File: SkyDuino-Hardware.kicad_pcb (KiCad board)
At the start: 4 copper layers, 123 x 56 mm, 75 parts, among them J1 24V, J11 DBG, J12 USB-A RMT, J13 DISP, J14 USB_C Artisan, J2 BT, J4 Drum, J5 Exhaust, J6 Cooling, J7 Cooling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

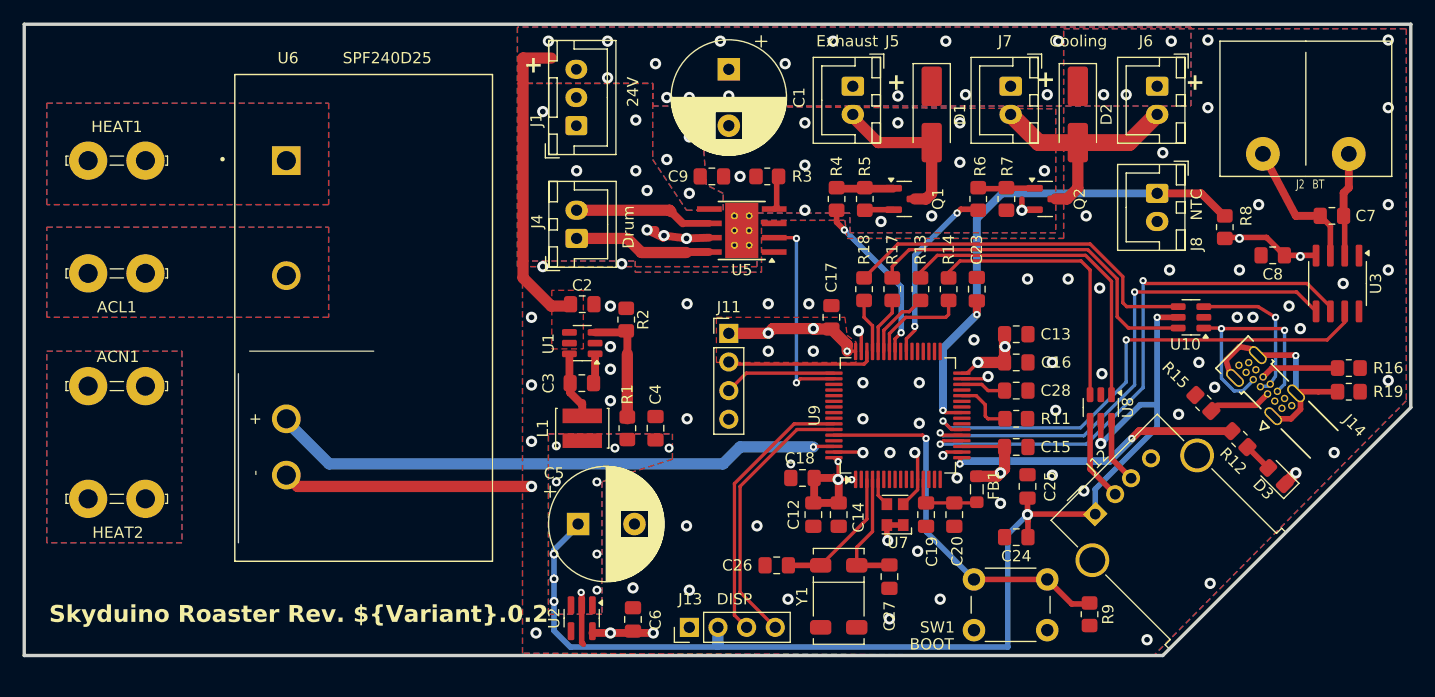
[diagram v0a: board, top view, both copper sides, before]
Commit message: Refactor power rail and optimize pours
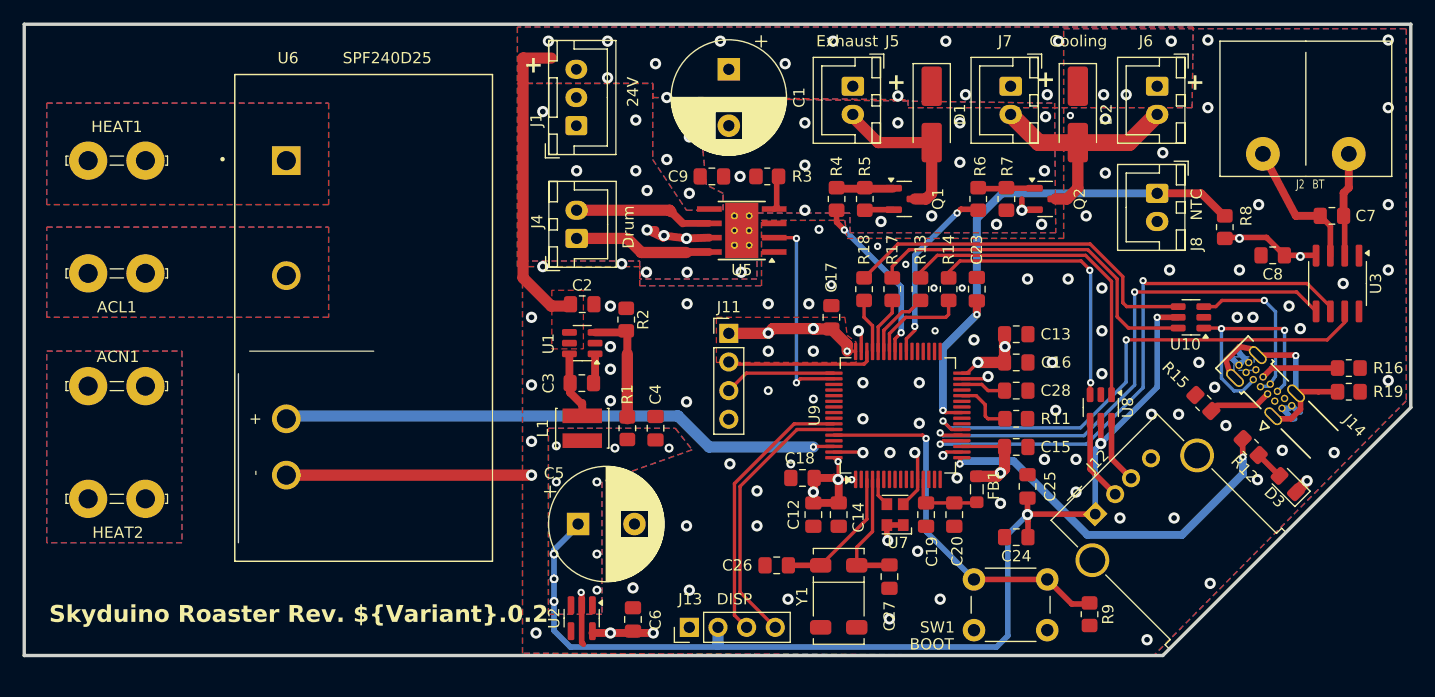
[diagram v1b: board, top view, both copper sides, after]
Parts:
- moved D3 1.22 mm to (218.1, 120.8)
- moved R12 1.22 mm to (214.8, 117.5)
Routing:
- net LED0: track 25.9 -> 33.9 mm
- net +5V: track 104.6 -> 97.6 mm
- net GND: track 52.7 -> 58.5 mm, vias 89 -> 117
- net SSR: track 51.0 -> 49.8 mm
- net /CPU/D+: track 13.7 -> 14.6 mm
- net Net-(R14-Pad1): vias 0 -> 2
- net +3V3: vias 16 -> 17
- net +24V: vias 21 -> 19

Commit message: Move SSR GND connection to B layer
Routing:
- net GND: vias 117 -> 119
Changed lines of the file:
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@@
 		)
 	)
+	(dimension
+		(type aligned)
+		(layer "F.Cu")
+		(pts
+			(xy 229 80) (xy 229 114)
+		)
+		(height -4.6)
+		(gr_text "34.0000 mm"
+			(at 231.8 97 90)
+			(layer "F.Cu")
+			(effects
+				(font
+					(size 1.5 1.5)
+					(thickness 0.3)
+				)
+			)
+		)
+		(format
+			(prefix "")
+			(suffix "")
+			(units 3)
+			(units_format 1)
+			(precision 4)
+		)
+		(style
+			(thickness 0.2)
+			(arrow_length 1.27)
+			(text_position_mode 0)
+			(extension_height 0.58642)
+			(extension_offset 0.5) keep_text_aligned)
+	)
+	(dimension
+		(type aligned)
+		(layer "F.Cu")
+		(pts
+			(xy 207.114627 135.504071) (xy 106 136)
+		)
+		(height -4.964587)
+		(gr_text "101.1158 mm"
+			(at 156.572834 138.916585 0.2810124376)
+			(layer "F.Cu")
+			(effects
+				(font
+					(size 1.5 1.5)
+					(thickness 0.3)
+				)
+			)
+		)
+		(format
+			(prefix "")
+			(suffix "")
+			(units 3)
+			(units_format 1)
+			(precision 4)
+		)
+		(style
+			(thickness 0.2)
+			(arrow_length 1.27)
+			(text_position_mode 0)
+			(extension_height 0.58642)
+			(extension_offset 0.5) keep_text_aligned)
+	)
+	(dimension
+		(type aligned)
+		(layer "F.Cu")
+		(pts
+			(xy 106 80) (xy 229 80)
+		)
+		(height -5)
+		(gr_text "123.0000 mm"
+			(at 167.5 73.2 0)
+			(layer "F.Cu")
+			(effects
+				(font
+					(size 1.5 1.5)
+					(thickness 0.3)
+				)
+			)
+		)
+		(format
+			(prefix "")
+			(suffix "")
+			(units 3)
+			(units_format 1)
+			(precision 4)
+		)
+		(style
+			(thickness 0.2)
+			(arrow_length 1.27)
+			(text_position_mode 0)
+			(extension_height 0.58642)
+			(extension_offset 0.5) keep_text_aligned)
+	)
+	(dimension
+		(type aligned)
+		(layer "F.Cu")
+		(pts
+			(xy 106 80) (xy 106 136)
+		)
+		(height 6.6)
+		(gr_text "56.0000 mm"
+			(at 97.6 108 90)
+			(layer "F.Cu")
+			(effects
+				(font
+					(size 1.5 1.5)
+					(thickness 0.3)
+				)
+			)
+		)
+		(format
+			(prefix "")
+			(suffix "")
+			(units 3)
+			(units_format 1)
+			(precision 4)
+		)
+		(style
+			(thickness 0.2)
+			(arrow_length 1.27)
+			(text_position_mode 0)
+			(extension_height 0.58642)
+			(extension_offset 0.5) keep_text_aligned)
+	)
 	(segment
 		(start 111.67 122.1)
@@
 	)
 	(segment
-		(start 151 120)
-		(end 129.25 120)
-		(width 1)
-		(layer "F.Cu")
-		(net 3)
-	)
-	(segment
 		(start 164.75 99)
 		(end 162.75 98.75)
@@
 	)
 	(via
+		(at 151 129)
+		(size 1)
+		(drill 0.5)
+		(layers "F.Cu" "B.Cu")
+		(free yes)
+		(net 3)
+	)
+	(via
 		(at 165 130.2)
 		(size 1)
@@
 	)
 	(via
+		(at 151 124)
+		(size 1)
+		(drill 0.5)
+		(layers "F.Cu" "B.Cu")
+		(free yes)
+		(net 3)
+	)
+	(via
 		(at 189.2 103.4)
 		(size 0.65)
@@
 	)
 	(segment
+		(start 151 120)
+		(end 129.25 120)
+		(width 1)
+		(layer "B.Cu")
+		(net 3)
+	)
+	(segment
 		(start 217.568377 114.068376)
 		(end 218.500001 115)
@@
 	)
 	(zone
-		(net 3)
-		(net_name "GND")
-		(layer "F.Cu")
-		(name "$teardrop_padvia$")
-		(hatch full 0.1)
-		(priority 30000)
-		(attr
-			(teardrop
-				(type padvia)
-			)
-		)
-		(connect_pads yes
-			(clearance 0)
-		)
-		(min_thickness 0.0254)
-		(filled_areas_thickness no)
-		(fill yes
-			(thermal_gap 0.5)
-			(thermal_bridge_width 0.5)
-			(island_removal_mode 1)
-			(island_area_min 10)
-		)
-		(polygon
-			(pts
-				(xy 131.525 120.5) (xy 131.525 119.5) (xy 130.011659 119) (xy 129.249 120) (xy 130.011659 121)
-			)
-		)
-	)
-	(zone
 		(net 10)
 		(net_name "Net-(J2-Pin_2)")
@@
 	)
 	(zone
-		(net 59)
-		(net_name "SSR")
+		(net 3)
+		(net_name "GND")
 		(layer "B.Cu")
 		(name "$teardrop_padvia$")
@@
 		(polygon
 			(pts
-				(xy 131.480918 115.25) (xy 131.480918 114.25) (xy 129.915266 113.919117) (xy 129.249 115) (xy 130.120549 115.90863)
+				(xy 131.525 120.5) (xy 131.525 119.5) (xy 130.011659 119) (xy 129.249 120) (xy 130.011659 121)
 			)
 		)
@@
 			)
 		)
+	)
+	(zone
+		(net 59)
+		(net_name "SSR")
+		(layer "B.Cu")
+		(name "$teardrop_padvia$")
+		(hatch full 0.1)
+		(priority 30000)
+		(attr
+			(teardrop
+				(type padvia)
+			)
+		)
+		(connect_pads yes
+			(clearance 0)
+		)
+		(min_thickness 0.0254)
+		(filled_areas_thickness no)
+		(fill yes
+			(thermal_gap 0.5)
+			(thermal_bridge_width 0.5)
+			(island_removal_mode 1)
+			(island_area_min 10)
+		)
+		(polygon
+			(pts
+				(xy 131.480918 115.25) (xy 131.480918 114.25) (xy 129.915266 113.919117) (xy 129.249 115) (xy 130.120549 115.90863)
+			)
+		)

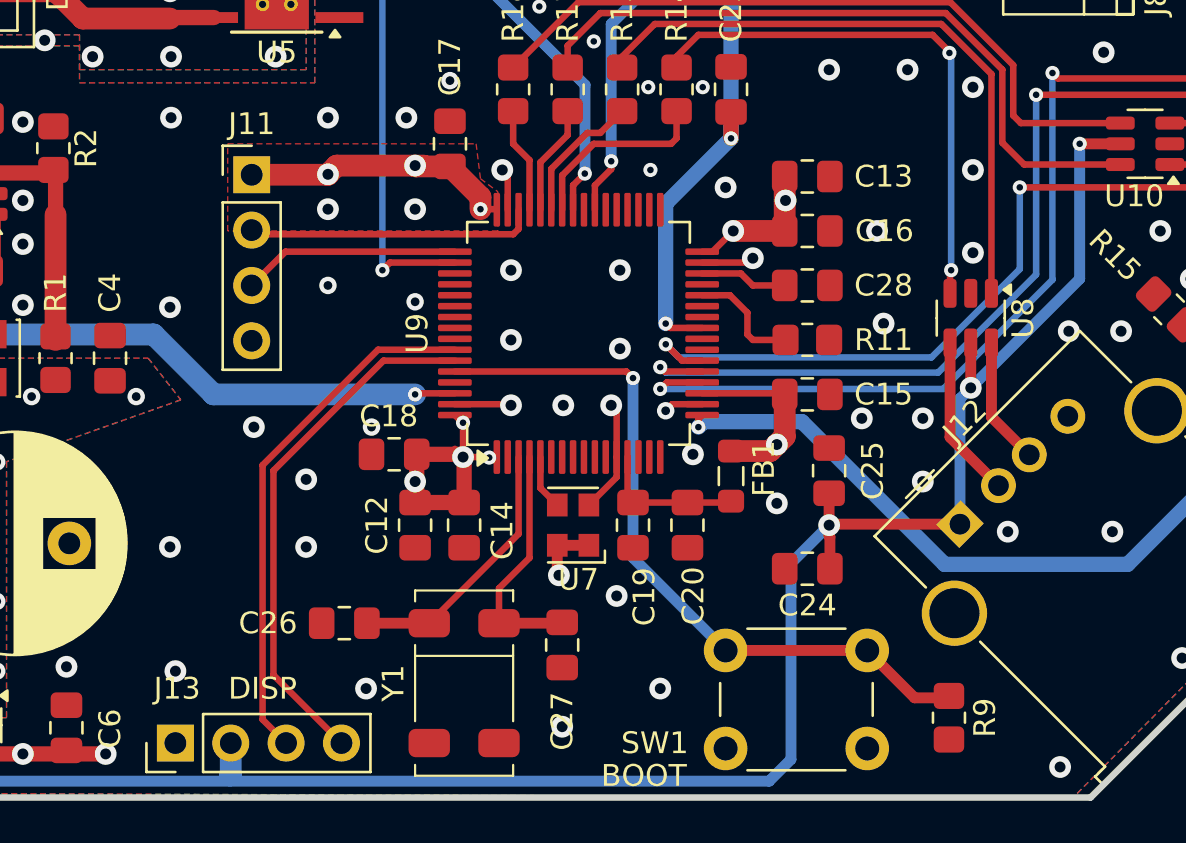
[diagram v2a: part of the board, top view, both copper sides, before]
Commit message: Add silkscreen for DBG/DISP
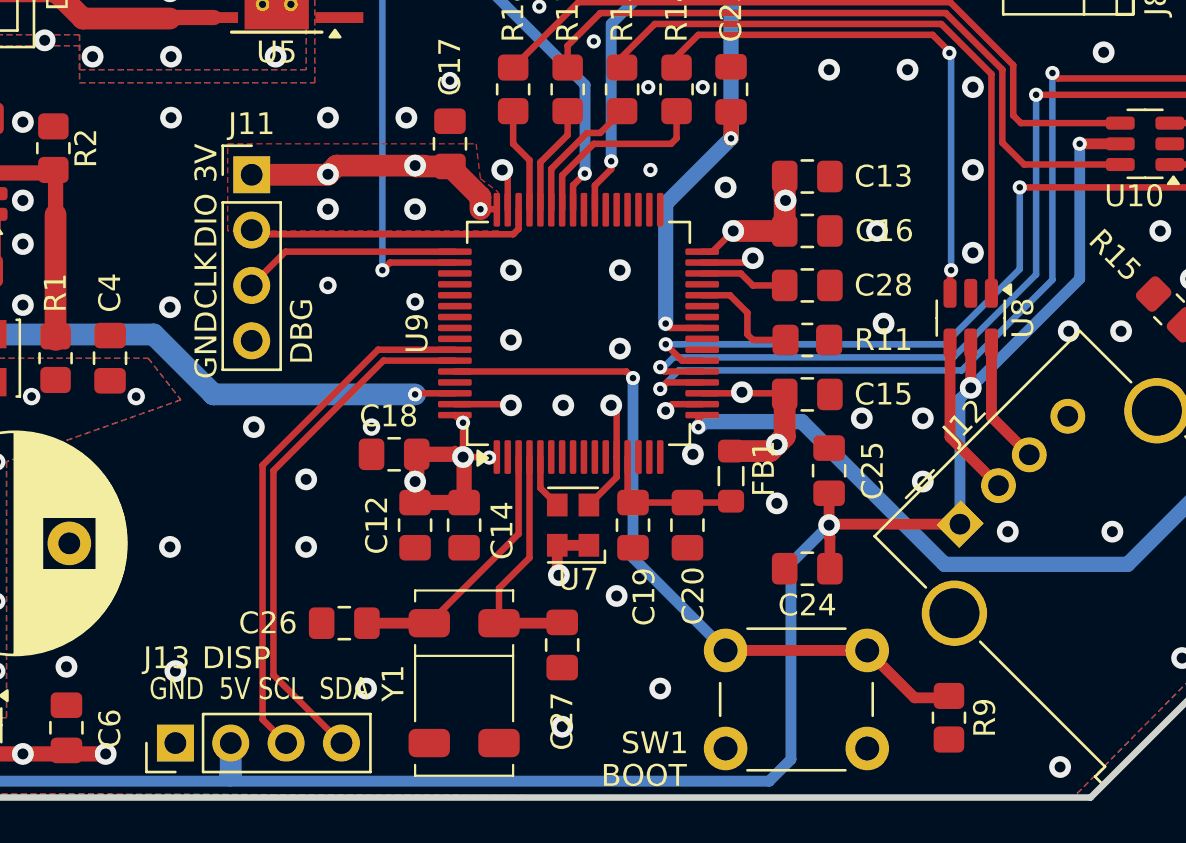
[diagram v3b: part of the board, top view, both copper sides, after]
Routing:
- net +3V3: vias 17 -> 18
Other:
- board text added: "3V"
- board text added: "5V"
- board text added: "CLK"
- board text added: "DIO"
- board text added: "GND"
- board text added: "SCL"
- board text added: "SDA"

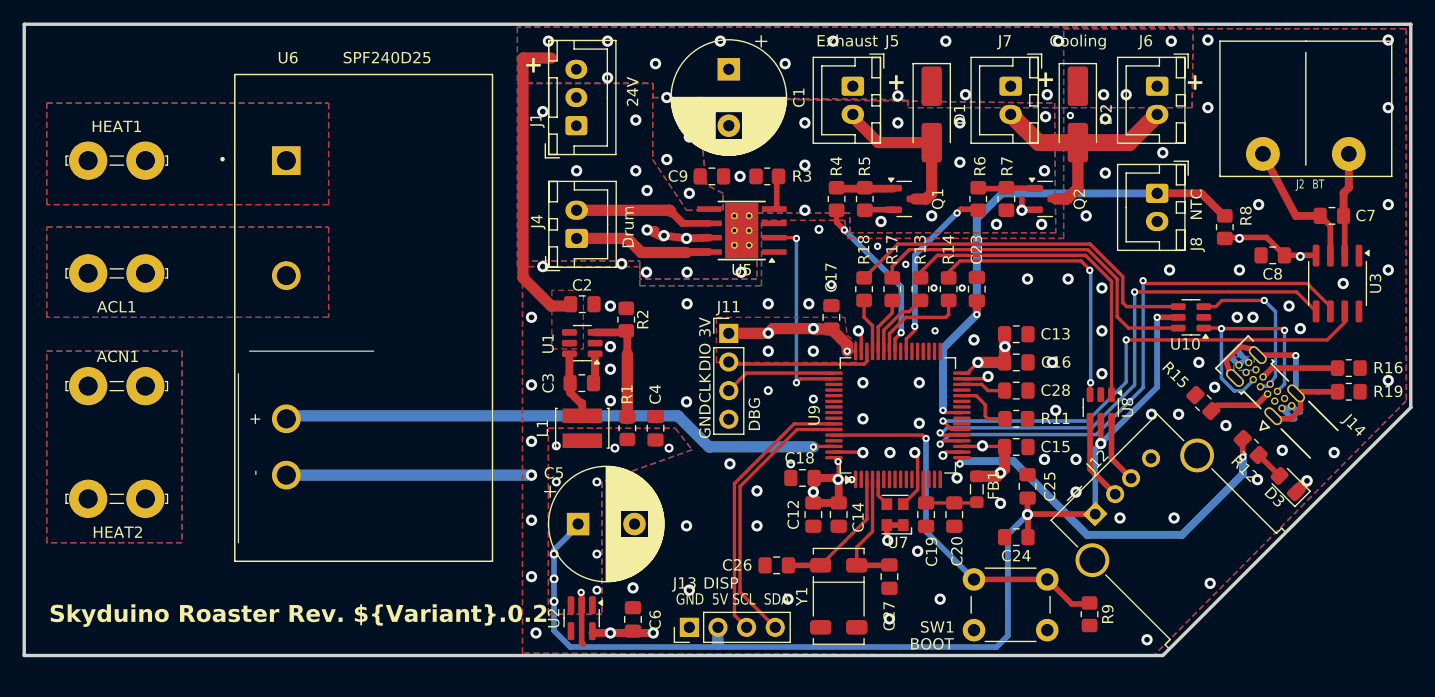
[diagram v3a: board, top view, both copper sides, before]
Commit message: Add Heat Safety relay
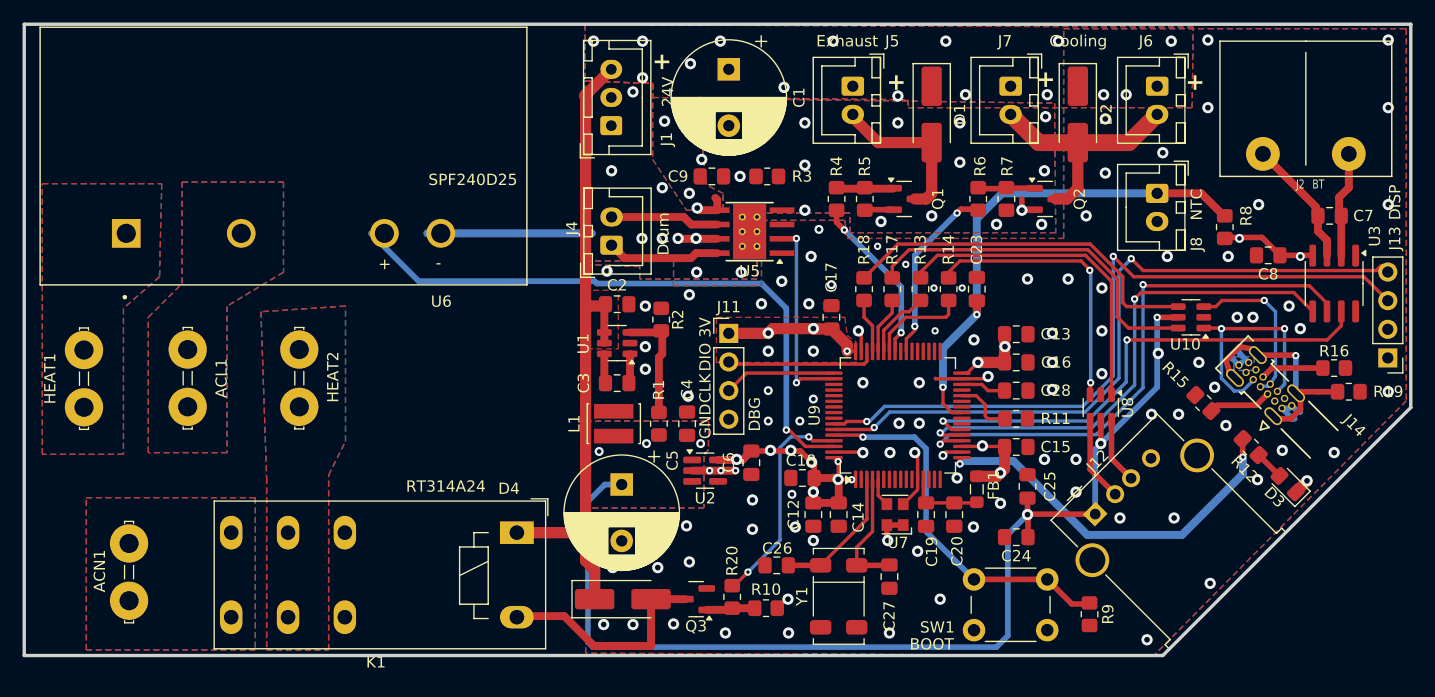
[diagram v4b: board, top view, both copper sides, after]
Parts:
- added D4: M2, Diode_SMD:D_SMA_Handsoldering, F.Cu at (159.1, 131.0)
- added K1: RT314A24, Relay_THT:Relay_SPDT_Schrack-RT1-16A-FormC_RM5mm, F.Cu at (149.7, 125.1)
- added Q3: DMN6075S, Package_TO_SOT_SMD:SOT-23, F.Cu at (165.6, 131.0)
- added R10: 10kΩ, Resistor_SMD:R_0805_2012Metric_Pad1.20x1.40mm_HandSolder, F.Cu at (171.8, 131.8)
- added R20: 100Ω, Resistor_SMD:R_0805_2012Metric_Pad1.20x1.40mm_HandSolder, F.Cu at (168.8, 130.8)
- C3: value 0.1µF -> 100nF
- C4: value 22uF -> 22µF
- C5: value 100uF -> 100µF
- moved J13 66.4 mm to (227.0, 109.6), turned to 180 degrees
- moved HEAT1 19.6 mm to (111.3, 111.4), turned to 90 degrees
- moved HEAT2 19.4 mm to (130.4, 111.4), turned to 90 degrees
- moved C6 17.4 mm to (170.5, 118.9), turned to -90 degrees
- moved U2 17.1 mm to (166.4, 119.6), turned to 0 degrees
- moved ACN1 16.5 mm to (115.3, 128.6), turned to 90 degrees
- moved ACL1 11.2 mm to (120.5, 111.4), turned to 90 degrees
- moved U6 7.50 mm to (129.0, 98.6), turned to 0 degrees
- moved C5 5.22 mm to (159.0, 120.8), turned to -90 degrees
- moved J4 3.16 mm to (158.1, 99.6)
- moved C3 3.14 mm to (158.6, 111.8)
- moved C2 3.10 mm to (158.6, 104.8)
- moved J1 3.10 mm to (158.1, 89.0)
- moved R2 3.10 mm to (162.5, 106.2)
- moved U1 3.10 mm to (158.6, 108.3)
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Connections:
- HEAT2 pad 1: Net-(ACN1-Pin_1) -> Net-(HEAT2-Pin_1)
- U9 pad 61: unconnected-(U9-PB8-Pad61) -> HEAT_CTL
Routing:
- net SCL: track 24.2 -> 63.1 mm, vias 0 -> 2
- net SDA: track 24.2 -> 61.8 mm, vias 0 -> 2
- net +24V: track 27.2 -> 62.9 mm
- net +5V: track 97.6 -> 120.4 mm, vias 13 -> 7
- net HEAT: track 0.00 -> 20.3 mm
- net HEAT_CTL: track 0.00 -> 19.4 mm, vias 0 -> 2
- net GND: track 58.5 -> 49.6 mm, vias 119 -> 122
- net SSR: track 49.8 -> 55.2 mm
- net +3V3: track 59.1 -> 63.9 mm, vias 18 -> 20
- net Net-(Q3-G): track 0.00 -> 4.32 mm
- net Net-(U1-SW): track 5.97 -> 2.71 mm
- net Net-(U5-ILIM): track 3.02 -> 0.11 mm
- net Net-(J4-Pin_2): track 12.3 -> 9.65 mm
- net Net-(J4-Pin_1): track 12.3 -> 10.0 mm
- net Net-(J14-CC2): track 6.93 -> 5.63 mm
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- added copper zone on B.Cu, net Net-(HEAT2-Pin_1)
- added copper zone on F.Cu, net Net-(HEAT2-Pin_1)
- added copper zone on In1.Cu, net Net-(HEAT2-Pin_1)
- added copper zone on In2.Cu, net Net-(HEAT2-Pin_1)
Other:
- outline, holes or cut-outs redrawn

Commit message: WIP DRC
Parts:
- moved C23 0.70 mm to (191.2, 103.5)
- moved C25 0.36 mm to (195.0, 121.4)
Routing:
- net NTC: track 44.7 -> 39.6 mm
- net Net-(U1-SW): track 2.71 -> 6.40 mm
- net Net-(U5-ILIM): track 0.11 -> 3.23 mm
- net GND: track 49.6 -> 50.9 mm, vias 122 -> 125
- net +24V: track 62.9 -> 64.0 mm
- net SSR: track 55.2 -> 54.7 mm
- net /CPU/XTAL_32K768_1: track 12.2 -> 12.7 mm
